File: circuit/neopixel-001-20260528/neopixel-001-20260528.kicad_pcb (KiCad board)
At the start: 2 copper layers, 114.3 x 114.3 mm, 67 parts, among them J1 Conn_NeoPixel, J2 Conn_01x02_Pin, J3 Conn_01x02_Pin, P1 ESP32C3_{1}, P10 unitV3, P11 unitV4, P12 unitV4, P2 ESP32C3_{1}, P3 ESP32C3_{2}, P4 ESP32C3_{2}, P5 unitV1, P6 unitV1, P7 unitV2, P8 unitV2, P9 unitV3, SW1 SW_SPST_LED, SW2 SW_SPST_LED, SW3 SW_SPST_LED, SW4 SW_SPST_LED, U1 SSD1306, U2 Aexit_0-50_Voltmeter

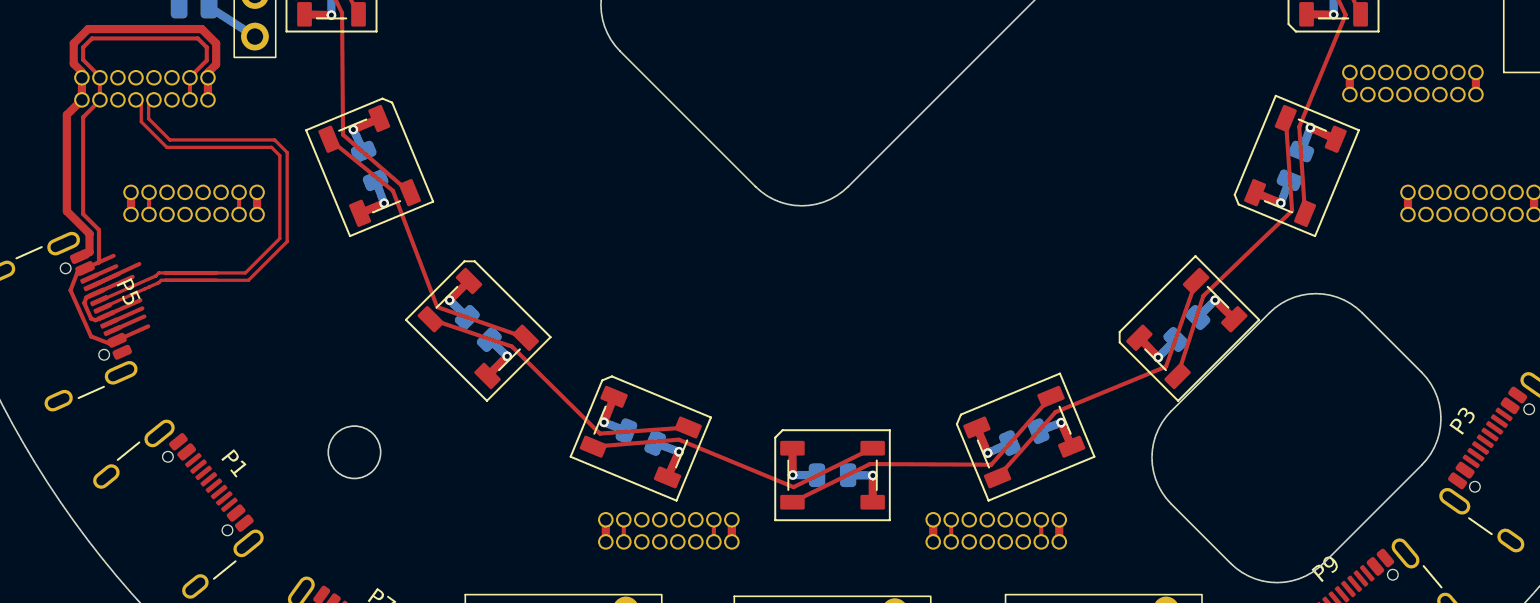
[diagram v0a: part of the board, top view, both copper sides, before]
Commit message: Update NeoPixel基板の差動配線を修正
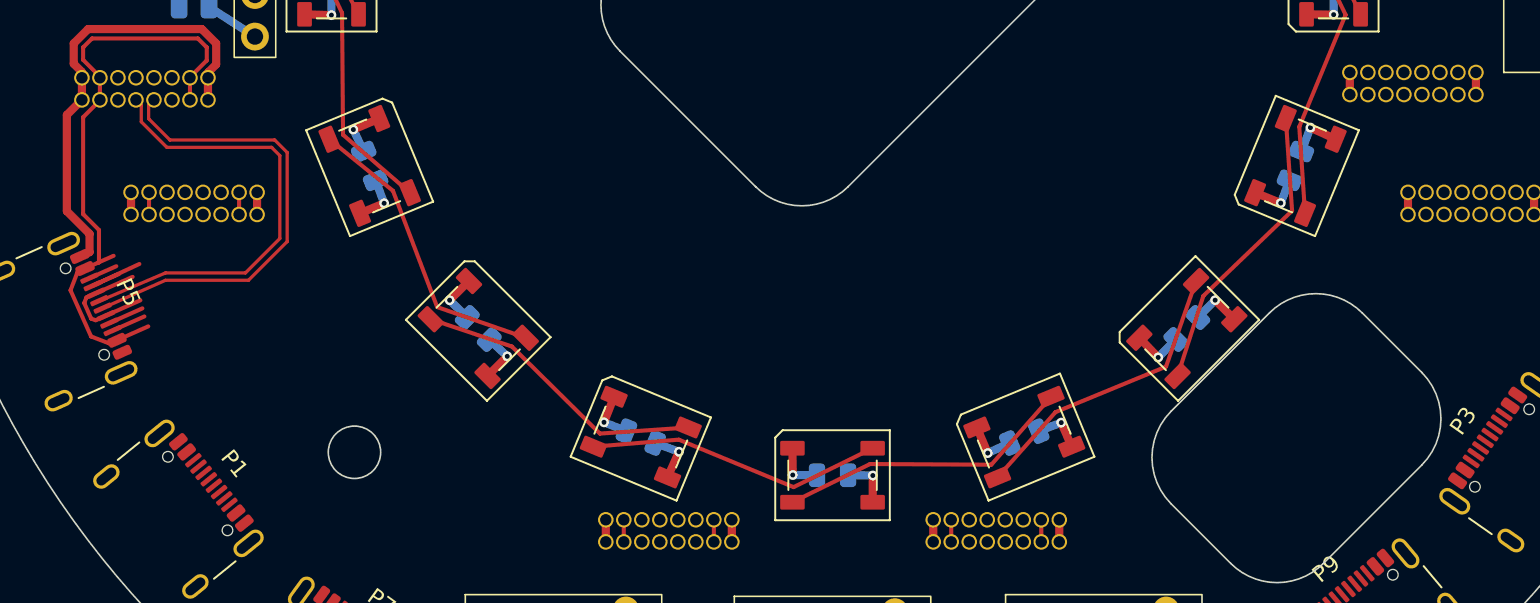
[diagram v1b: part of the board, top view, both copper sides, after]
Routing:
- net P3_D-: track 31.3 -> 28.1 mm
- net P3_D+: track 31.8 -> 28.7 mm

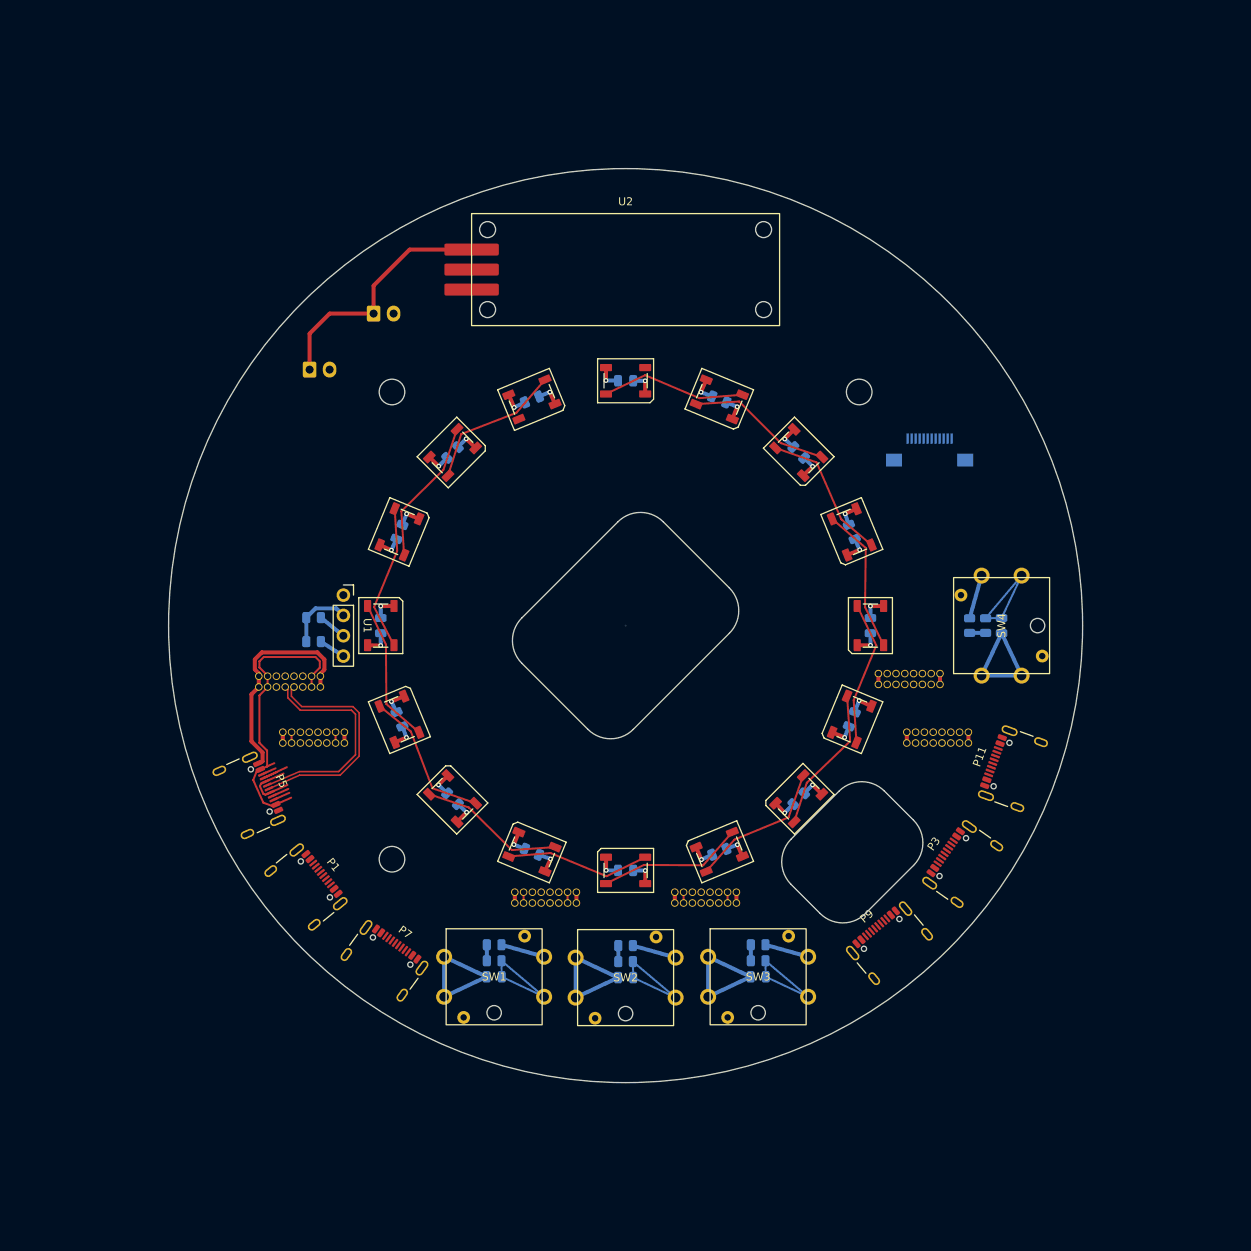
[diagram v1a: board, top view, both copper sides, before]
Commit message: Update ネオピクセル基板のPCBを進めた。未配線残り5
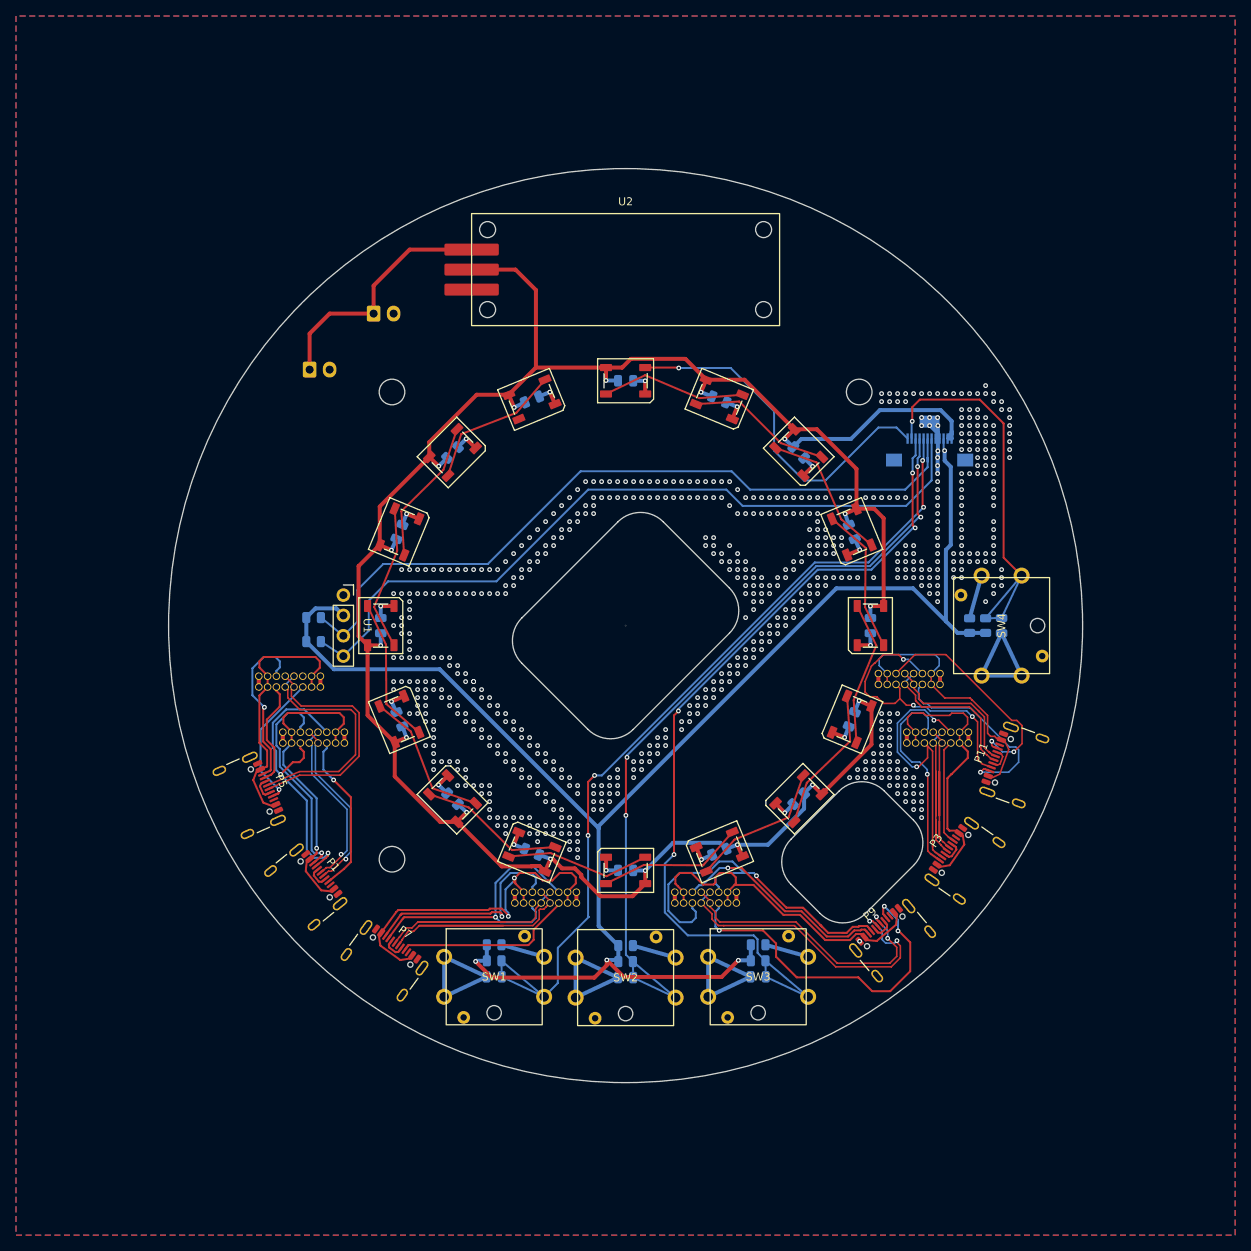
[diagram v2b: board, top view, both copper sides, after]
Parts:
- moved P3 0.50 mm to (43.3, 30.0)
- moved P9 0.50 mm to (34.1, 40.2)
- moved P11 0.50 mm to (49.6, 17.8)
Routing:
- net +5V: track 50.5 -> 302.5 mm
- net +3.3V: track 16.5 -> 204.3 mm, vias 0 -> 4
- net SW_{TCT1}: track 14.8 -> 108.9 mm, vias 0 -> 4
- net SW_{TCT3}: track 14.8 -> 107.5 mm, vias 0 -> 4
- net SDA: track 3.34 -> 95.1 mm
- net SCL: track 3.61 -> 93.7 mm
- net SW_{TCT2}: track 14.8 -> 100.2 mm, vias 0 -> 4
- net P5_CC: track 0.00 -> 46.9 mm, vias 0 -> 1
- net SIG_{NeoPixel}: track 0.00 -> 44.8 mm, vias 0 -> 1
- net P5_SBU1: track 0.00 -> 44.1 mm, vias 0 -> 3
- net P4_VBUS: track 2.70 -> 46.6 mm, vias 0 -> 2
- net P5_VBUS: track 2.70 -> 43.0 mm
- net P5_D-: track 0.00 -> 39.9 mm, vias 0 -> 2
- net P1_CC: track 0.00 -> 37.8 mm, vias 0 -> 2
- net SW_{START}: track 14.8 -> 51.8 mm, vias 0 -> 1
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- added copper zone on B.Cu, net GND
- added copper zone on F.Cu, net GND

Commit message: Update ネオピクセル基板のPCBを完成させた
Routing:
- net P3_CC: track 13.3 -> 31.9 mm, vias 0 -> 1
- net GND: track 155.0 -> 168.9 mm, vias 654 -> 941
- net P1_VBUS: track 38.8 -> 41.4 mm
- net P1_SBU2: track 27.1 -> 28.9 mm
- net P1_CC: track 37.8 -> 36.2 mm

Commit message: Update ネオピクセル基板のコンポーネントコンポーネント再度仮配置。時間返せ
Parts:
- P10, P12, P2, P4, P6, P8: footprint @Thrive_footprint_neopixel:USB_Type-C_Vertical_ C6332304 -> Connector_USB:USB_C_Receptacle_GCT_USB4105-xx-A_16P_TopMnt_Horizontal
- moved P12 19.8 mm to (29.6, -12.2), turned to 112.5 degrees
- moved P2 18.5 mm to (-22.6, 22.6), turned to -45 degrees
- moved P4 15.7 mm to (32.0, 0.00), turned to 90 degrees
- moved P6 13.5 mm to (-29.6, 12.2), turned to -67.5 degrees
- moved P10 10.2 mm to (0.00, 32.0)
- moved P8 4.97 mm to (-12.2, 29.6), turned to -22.5 degrees
- moved C8 2.71 mm to (9.00, 28.3)
- moved C7 1.92 mm to (23.0, 23.0)
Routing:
- net P5_CC: track 46.9 -> 0.00 mm, vias 1 -> 0
- net P5_SBU1: track 44.1 -> 0.00 mm, vias 3 -> 0
- net P4_VBUS: track 46.6 -> 6.50 mm, vias 2 -> 0
- net P5_D-: track 39.9 -> 0.04 mm, vias 2 -> 0
- net P4_CC: track 36.6 -> 0.00 mm, vias 1 -> 0
- net P5_VBUS: track 43.0 -> 6.54 mm
- net P5_D+: track 36.4 -> 0.04 mm, vias 2 -> 0
- net P1_CC: track 36.2 -> 0.00 mm, vias 2 -> 0
- net P6_CC: track 36.1 -> 0.00 mm, vias 3 -> 0
- net P2_CC: track 34.9 -> 0.00 mm, vias 2 -> 0
- net P1_VBUS: track 41.4 -> 6.50 mm, vias 1 -> 0
- net P4_D+: track 34.4 -> 0.00 mm
- net P6_VBUS: track 33.9 -> 0.00 mm
- net P4_D-: track 33.9 -> 0.00 mm
- net P3_VBUS: track 33.5 -> 0.00 mm
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
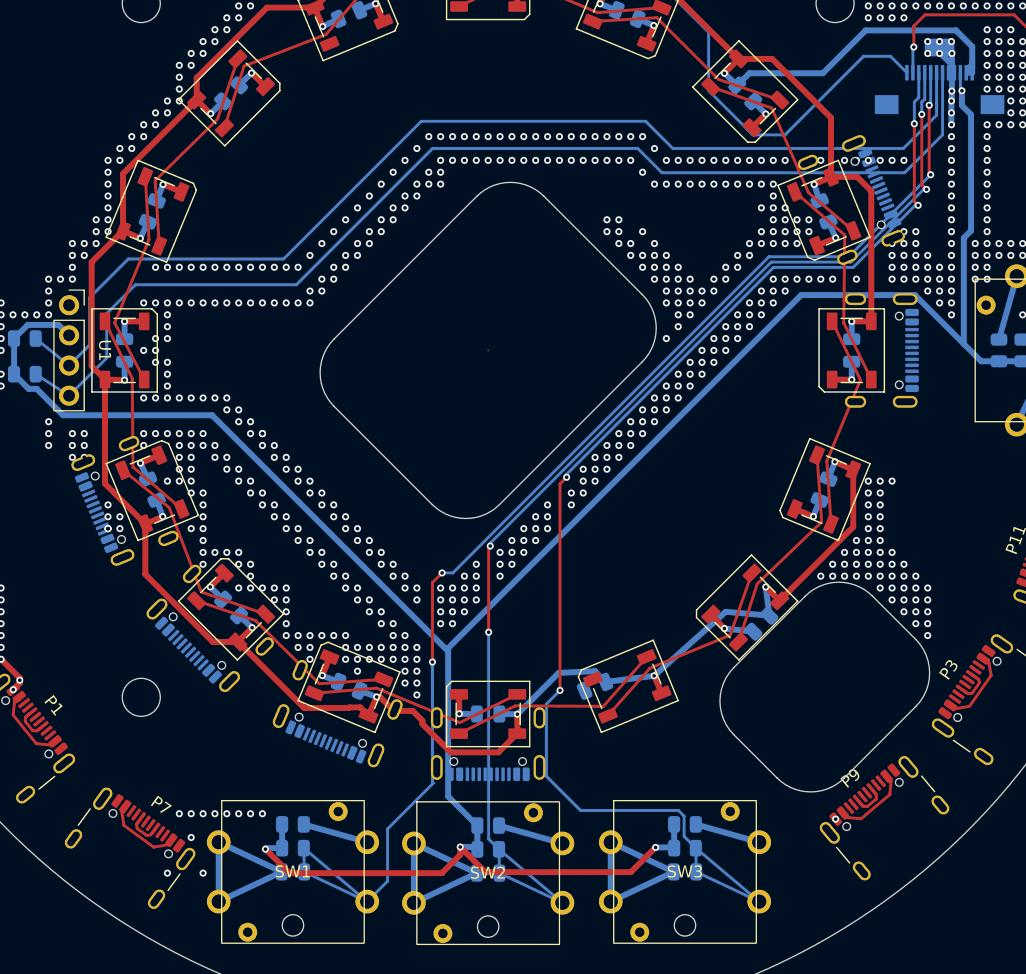
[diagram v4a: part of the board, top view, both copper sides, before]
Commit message: Update ネオピクセル基板のコンポーネントを再配置した。明日配線する。もう今日か
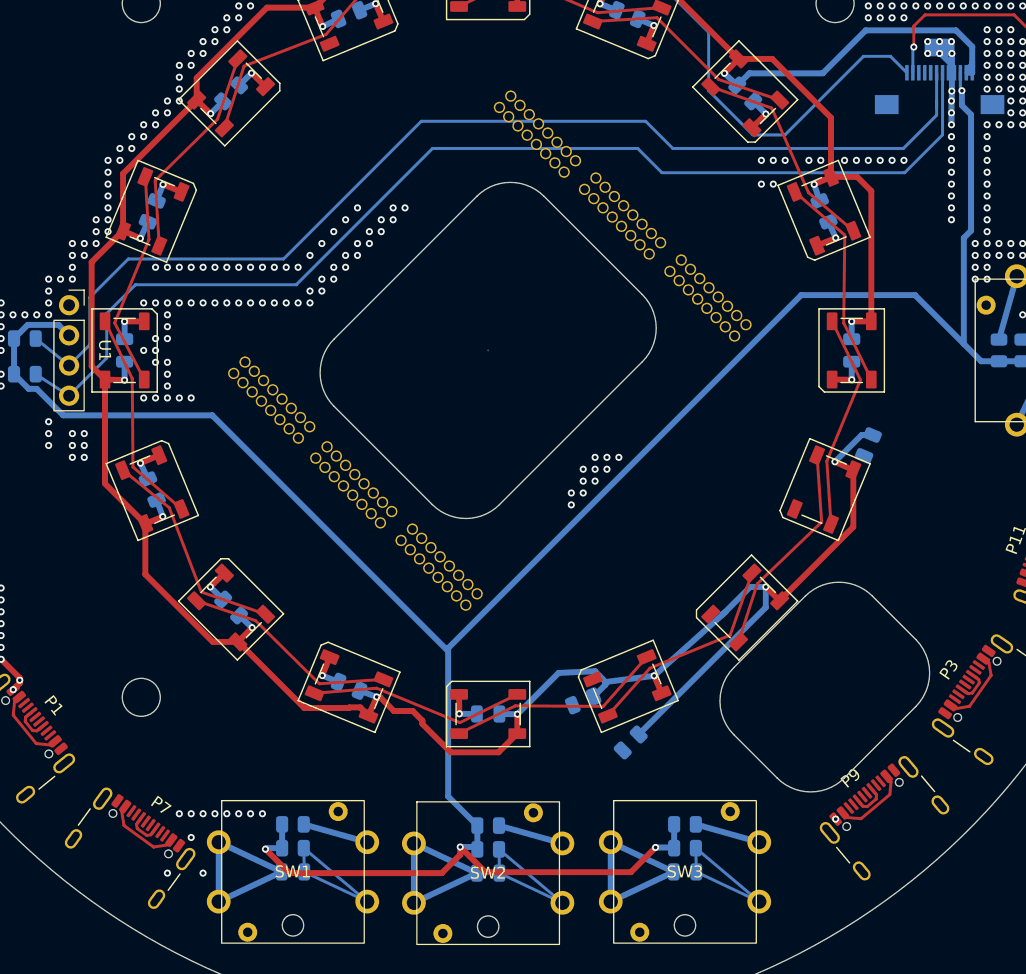
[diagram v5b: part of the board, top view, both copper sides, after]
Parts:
- P10, P12, P2, P4, P6, P8: footprint Connector_USB:USB_C_Receptacle_GCT_USB4105-xx-A_16P_TopMnt_Horizontal -> @Thrive_footprint_neopixel:USB_Type-C_Vertical_ C6332304
- moved P10 40.8 mm to (18.5, -4.41), turned to 135 degrees
- moved P12 26.1 mm to (4.15, -18.2), turned to 135 degrees
- moved P4 23.6 mm to (11.3, -11.3), turned to 135 degrees
- moved P2 16.0 mm to (-11.3, 11.3)
- moved C7 14.9 mm to (12.0, 33.0)
- moved P8 13.9 mm to (-4.13, 18.2), turned to -45 degrees
- moved P6 13.9 mm to (-18.2, 4.18), turned to -45 degrees
- moved C6 5.26 mm to (32.0, 8.00)
- moved C8 1.58 mm to (8.00, 29.5)
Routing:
- net SW_{TCT1}: track 108.9 -> 14.8 mm, vias 4 -> 0
- net SW_{TCT3}: track 107.5 -> 14.8 mm, vias 4 -> 0
- net SW_{TCT2}: track 100.2 -> 14.8 mm, vias 4 -> 0
- net +5V: track 303.1 -> 322.6 mm
- net GND: track 144.5 -> 137.2 mm, vias 938 -> 506

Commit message: Update ネオピクセル基板のPCB完成した。干渉いけてくれ
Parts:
- moved P2 1.05 mm to (-12.0, 12.1)
- moved P4 0.40 mm to (11.6, -11.6)
- turned P10 to -45 degrees
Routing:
- net SW_{TCT3}: track 14.8 -> 148.8 mm, vias 0 -> 4
- net SW_{TCT2}: track 14.8 -> 120.3 mm, vias 0 -> 4
- net SW_{TCT1}: track 14.8 -> 114.8 mm, vias 0 -> 4
- net GND: track 137.2 -> 235.8 mm, vias 506 -> 138
- net P2_CC: track 0.00 -> 94.4 mm, vias 0 -> 2
- net P5_VBUS: track 6.54 -> 94.7 mm, vias 0 -> 2
- net P5_SBU2: track 0.00 -> 85.5 mm, vias 0 -> 3
- net P6_CC: track 0.00 -> 84.5 mm, vias 0 -> 4
- net P6_SBU2: track 0.00 -> 83.1 mm, vias 0 -> 1
- net P5_CC: track 0.00 -> 83.1 mm, vias 0 -> 2
- net P2_SBU2: track 0.00 -> 82.0 mm, vias 0 -> 1
- net +3.3V: track 204.3 -> 285.5 mm, vias 4 -> 10
- net P6_VBUS: track 0.00 -> 81.0 mm, vias 0 -> 4
- net P2_VBUS: track 6.54 -> 86.5 mm, vias 0 -> 1
- net P5_D+: track 0.04 -> 72.9 mm, vias 0 -> 1
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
